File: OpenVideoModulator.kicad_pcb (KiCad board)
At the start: 2 copper layers, 38.6 x 24.9 mm, 22 parts, among them J1 CONN_6, J2 S-Video+Composite_Combo, P1 OSHW_LOGO, U1 AD724, Y1 4.433619M

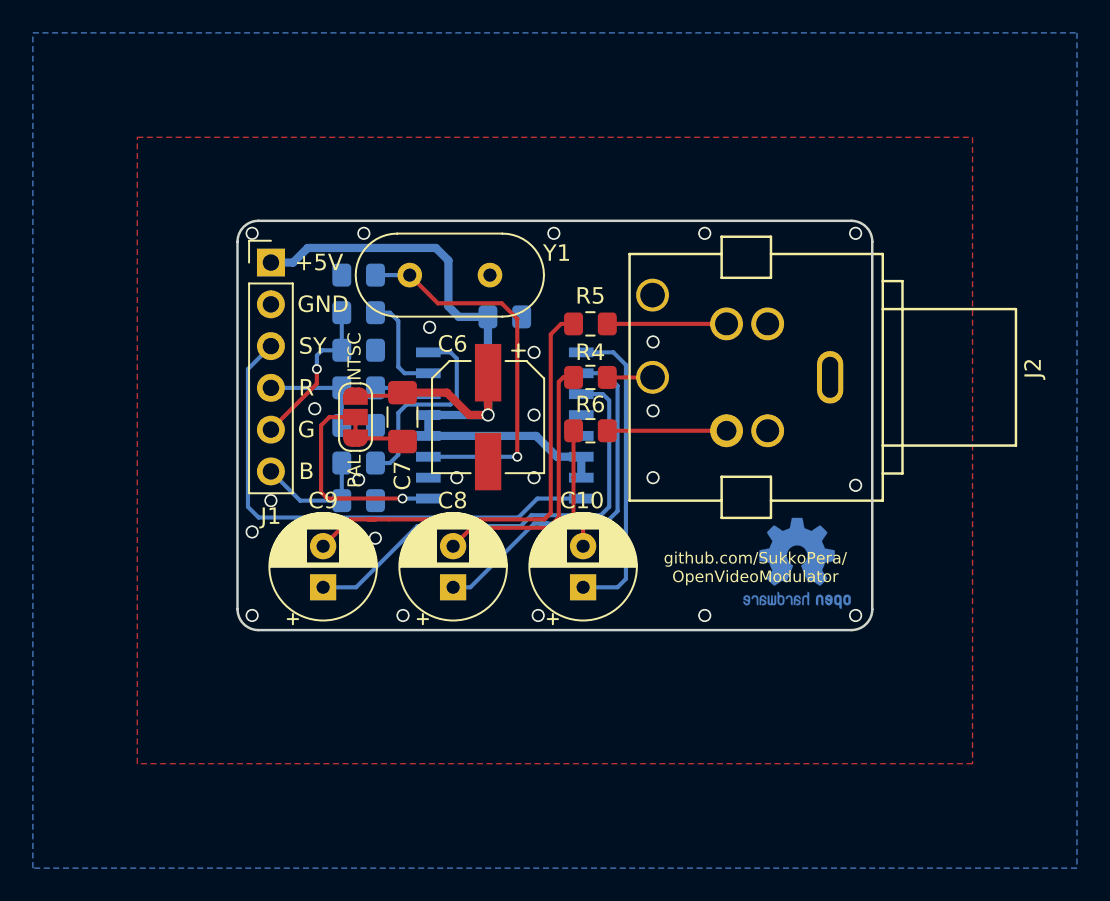
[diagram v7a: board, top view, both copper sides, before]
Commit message: V2 with RCA connector for composite video only
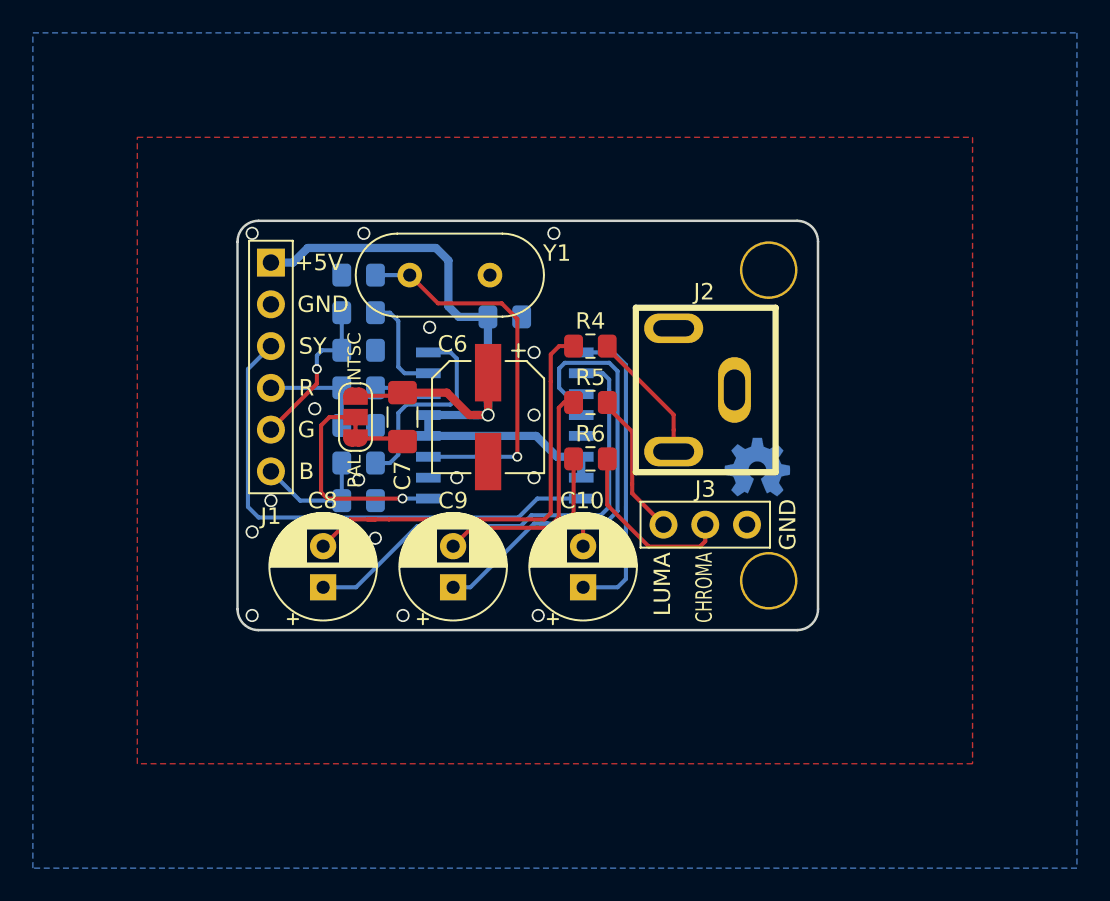
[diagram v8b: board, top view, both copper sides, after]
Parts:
- removed P1: OSHW_LOGO, Symbol:OSHW-Logo2_7.3x6mm_Copper
- added H1: MountingHole_Pad, MountingHole:MountingHole_3.2mm_M3_Pad, F.Cu at (148.1, 71.4)
- added H2: MountingHole_Pad, MountingHole:MountingHole_3.2mm_M3_Pad, F.Cu at (146.4, 52.8)
- added J3: SVIDEO_OUT, OpenVideoModulator:Pin_Header_Straight_1x03-ModSilkS, F.Cu at (145.0, 68.0)
- added V0: OSHW_LOGO, OpenVideoModulator:oshw_logo, B.Cu at (145.7, 64.5)
- J1: footprint Connector_PinHeader_2.54mm:PinHeader_1x06_P2.54mm_Vertical -> OpenVideoModulator:PinHeader_1x06_P2.54mm_Vertical
- J2: value S-Video+Composite_Combo -> VIDEOCOMP_OUT; footprint OpenVideoModulator:AV-MDC-401 -> OpenVideoModulator:SWITCHCRAFT_PJRAN1X1U01X
- moved J2 11.3 mm to (144.3, 59.8)
- moved C8 7.91 mm to (119.3, 71.8)
- moved C9 7.91 mm to (127.2, 71.8)
- moved R5 4.78 mm to (135.5, 60.6)
- moved R4 1.91 mm to (135.5, 57.1)
- moved R6 1.71 mm to (135.5, 64.0)
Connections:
- net Net-(C10-Pad1) renamed /chroma
- net Net-(C8-Pad1) renamed /composite
- net Net-(C9-Pad1) renamed /luma
- J2 pad 2: GND -> Net-(J2-Pad2)
- J2 pad 3: Net-(J2-Pad3) -> (no net)
- R4 pad 1: Net-(J2-Pad6) -> Net-(J2-Pad2)
- R5 pad 1: Net-(J2-Pad3) -> Net-(J3-Pad3)
- R6 pad 1: Net-(J2-Pad4) -> Net-(J3-Pad2)
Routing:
- net Net-(C9-Pad2): track 27.7 -> 14.9 mm
- net Net-(J3-Pad2): track 0.00 -> 11.0 mm
- net Net-(C8-Pad2): track 16.4 -> 26.4 mm
- net Net-(J3-Pad3): track 0.00 -> 9.11 mm
- net Net-(J2-Pad2): track 0.00 -> 8.09 mm
- net Net-(J2-Pad4): track 7.25 -> 0.00 mm
- net Net-(J2-Pad3): track 7.25 -> 0.00 mm
- net /composite: track 22.5 -> 29.4 mm
- net Net-(J2-Pad6): track 2.76 -> 0.00 mm
- net Net-(C10-Pad2): track 7.26 -> 5.55 mm
- net GND: vias 26 -> 18
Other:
- board size 38.6 x 24.9 mm -> 35.3 x 24.9 mm
- board text added: "CHROMA"
- board text added: "LUMA"
- board text added: "V2"
- board text removed: "V1"
